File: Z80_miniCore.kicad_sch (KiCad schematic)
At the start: 37 parts, among them J1 ICSP, J2 UART, J3 I2C, J7 USB_B_Mini, SW1 ON|OFF, SW2 Z80_RESET, U1 Z84C00/PLCC, U2 PIC1-MMU, U3 AS6C4008-55PCN, U4 SST39SF010, U5 74HC595, U6 74HC595, U7 74HC595, Y1 CANNED-DIP8, Y2 Crystal

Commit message: add footprints for 595 + SST39SF
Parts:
- U4: footprint (none) -> Package_DIP:DIP-32_W15.24mm
- U5, U6, U7: footprint (none) -> Package_DIP:DIP-16_W7.62mm
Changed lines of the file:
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@@
 			)
 		)
-		(property "Footprint" ""
+		(property "Footprint" "Package_DIP:DIP-16_W7.62mm"
 			(at 152.4 128.27 0)
 			(hide yes)
@@
 			)
 		)
-		(property "Footprint" ""
+		(property "Footprint" "Package_DIP:DIP-32_W15.24mm"
 			(at 172.72 49.53 0)
 			(hide yes)
@@
 			)
 		)
-		(property "Footprint" ""
+		(property "Footprint" "Package_DIP:DIP-16_W7.62mm"
 			(at 114.3 128.27 0)
 			(hide yes)
@@
 			)
 		)
-		(property "Footprint" ""
+		(property "Footprint" "Package_DIP:DIP-16_W7.62mm"
 			(at 77.47 128.27 0)
 			(hide yes)

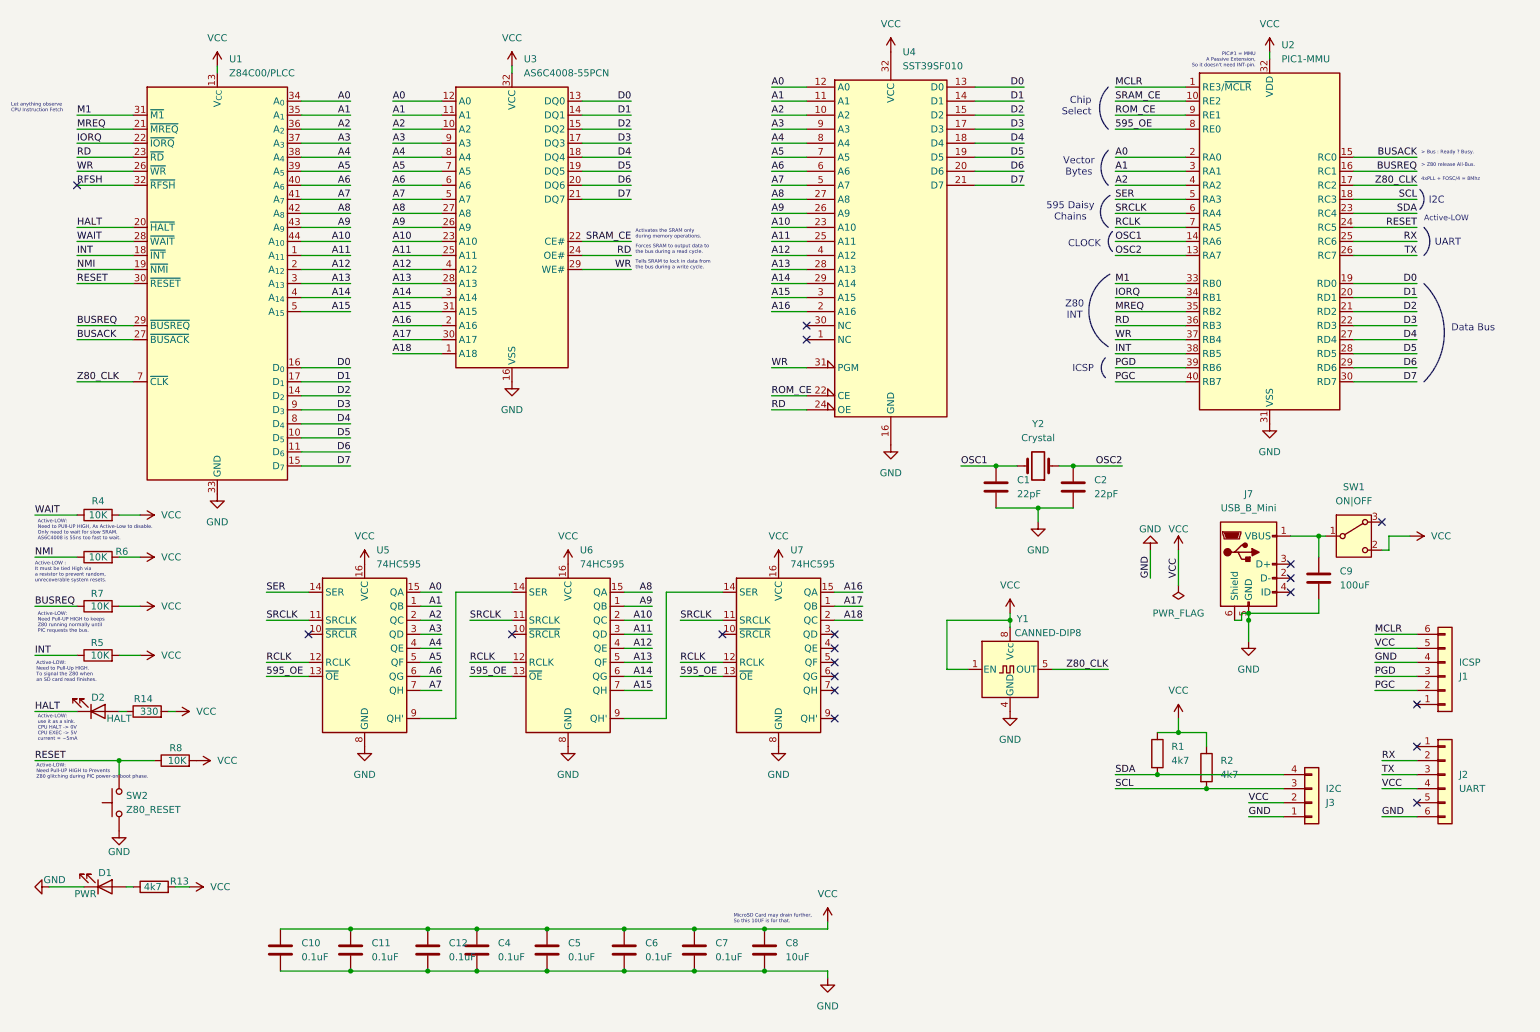
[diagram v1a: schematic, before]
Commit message: Remove Daisy Chain.
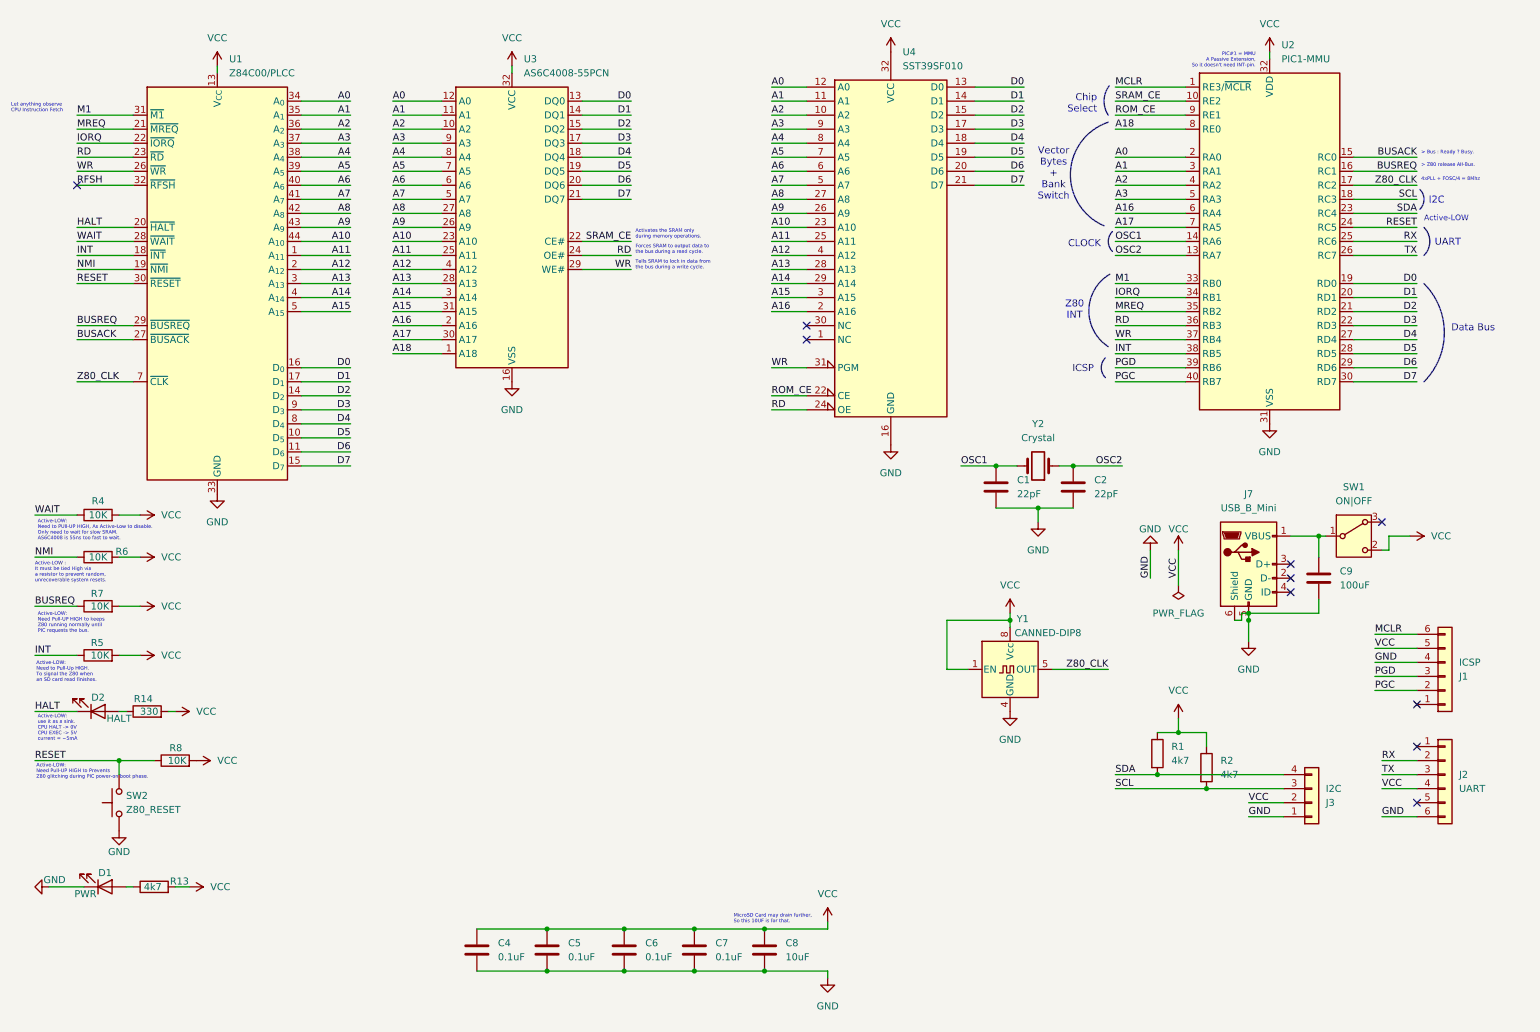
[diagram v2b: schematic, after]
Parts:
- removed C10, C11, C12: 0.1uF, Capacitor_THT:C_Disc_D3.4mm_W2.1mm_P2.50mm, symbol Device:C
- removed U5, U6, U7: 74HC595, Package_DIP:DIP-16_W7.62mm, symbol 74xx:74HC595
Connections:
- net 595_OE is gone; now on net A18: U2.8 (RE0)
- net RCLK is gone; now on net A17: U2.7 (RA5)
- net SER is gone; now on net A3: U2.5 (RA3)
- net SRCLK is gone; now on net A16: U2.6 (RA4)
- no-connect marks 19 -> 10
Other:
- note added: "Vector Bytes + Bank Switch"
- note removed: "595 Daisy Chains"
- note removed: "Vector Bytes"

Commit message: Add PIC2 as LOADER.
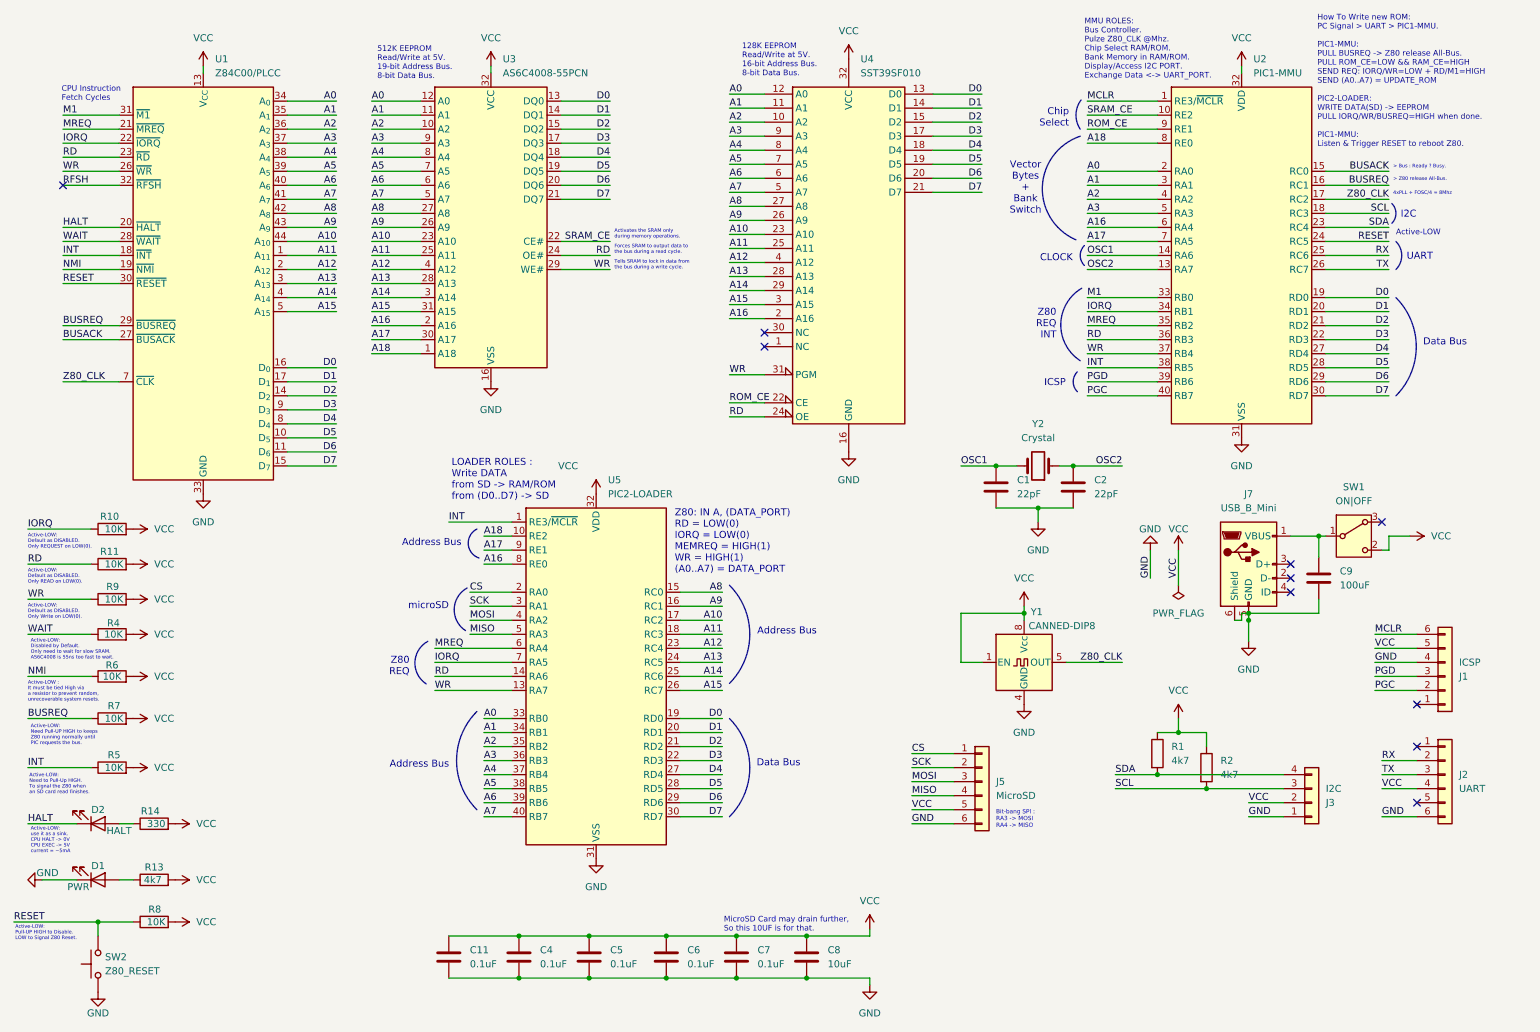
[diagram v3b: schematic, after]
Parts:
- added C11: 0.1uF, Capacitor_THT:C_Disc_D3.4mm_W2.1mm_P2.50mm, symbol Device:C
- added J5: MicroSD, Connector_PinSocket_2.54mm:PinSocket_1x06_P2.54mm_Vertical, symbol Connector_Generic:Conn_01x06
- added R10, R11, R9: 10K, Resistor_THT:R_Axial_DIN0207_L6.3mm_D2.5mm_P10.16mm_Horizontal, symbol Device:R
- added U5: PIC2-LOADER, Package_DIP:DIP-40_W15.24mm, symbol MCU_Microchip_PIC18:PIC18F4520-xP
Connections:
- net A0: now also U5.33 (RB0)
- net A1: now also U5.34 (RB1)
- net A10: now also U5.17 (RC2)
- net A11: now also U5.18 (RC3)
- net A12: now also U5.23 (RC4)
- net A13: now also U5.24 (RC5)
- net A14: now also U5.25 (RC6)
- net A15: now also U5.26 (RC7)
- net A16: now also U5.8 (RE0)
- net A17: now also U5.9 (RE1)
- net A18: now also U5.10 (RE2)
- net A2: now also U5.35 (RB2)
- net A3: now also U5.36 (RB3)
- net A4: now also U5.37 (RB4)
- net A5: now also U5.38 (RB5)
- net A6: now also U5.39 (RB6)
- net A7: now also U5.40 (RB7)
- net A8: now also U5.15 (RC0)
- net A9: now also U5.16 (RC1)
- net D0: now also U5.19 (RD0)
- net D1: now also U5.20 (RD1)
- net D2: now also U5.21 (RD2)
- net D3: now also U5.22 (RD3)
- net D4: now also U5.27 (RD4)
- net D5: now also U5.28 (RD5)
- net D6: now also U5.29 (RD6)
- net D7: now also U5.30 (RD7)
- net GND: now also C11.1, J5.6 (Pin_6), U5.12 (VSS), U5.31 (VSS)
- net INT: now also U5.1 (RE3/~{MCLR})
- net IORQ: now also R10.1, U5.7 (RA5)
- net MREQ: now also U5.6 (RA4)
- net RD: now also R11.1, U5.14 (RA6)
- net VCC: now also C11.2, J5.5 (Pin_5), R10.2, R11.2, R9.2, U5.11 (VDD), U5.32 (VDD)
- net WR: now also R9.1, U5.13 (RA7)
- new net CS: J5.1 (Pin_1), U5.2 (RA0)
- new net MISO: J5.4 (Pin_4), U5.5 (RA3)
- new net MOSI: J5.3 (Pin_3), U5.4 (RA2)
- new net SCK: J5.2 (Pin_2), U5.3 (RA1)
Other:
- note added: "128K EEPROM Read/Write at 5V. 16-bit Address Bus. 8-bit Data Bus."
- note added: "512K EEPROM Read/Write at 5V. 19-bit Address Bus. 8-bit Data Bus."
- note added: "Active-LOW: Default as DISABLED. Only READ on LOW(0)."
- note added: "Active-LOW: Default as DISABLED. Only REQUEST on LOW(0)."
- note added: "Active-LOW: Default as DISABLED. Only Write on LOW(0)."
- note added: "Active-LOW: Disabled by Default. Only need to wait for slow SRAM. AS6C4008 is 55ns too fast to wait."
- note added: "Active-LOW: Pull-UP HIGH to Disable. LOW to Signal Z80 Reset."
- note added: "Address Bus"
- note added: "Bit-bang SPI : RA3 -> MOSI RA4 -> MISO"
- note added: "CPU Instruction Fetch Cycles"
- note added: "How To Write new ROM: PC Signal > UART > PIC1-MMU. PIC1-MMU: PULL BUSREQ -> Z80 release All-Bus. PULL ROM_CE=LOW && RAM_CE=HIGH SEND REQ: IORQ/WR=LOW + RD/M1=HIGH SEND (A0..A7) = UPDATE_ROM PIC2-LOADER: WRITE DATA(SD) -> EEPROM PULL IORQ/WR/BUSREQ=HIGH when done. PIC1-MMU: Listen & Trigger RESET to reboot Z80."
- note added: "LOADER ROLES : Write DATA from SD -> RAM/ROM from (D0..D7) -> SD"
- note added: "MMU ROLES: Bus Controller. Pulze Z80_CLK @Mhz. Chip Select RAM/ROM. Bank Memory in RAM/ROM. Display/Access I2C PORT. Exchange Data <-> UART_PORT."
- note added: "Z80 REQ"
- note added: "Z80 REQ INT"
- note added: "Z80: IN A, (DATA_PORT) RD = LOW(0) IORQ = LOW(0) MEMREQ = HIGH(1) WR = HIGH(1) (A0..A7) = DATA_PORT"
- note added: "microSD"
- note removed: "Active-LOW: Need Pull-UP HIGH to Prevents Z80 glitching during PIC power-on boot phase."
- note removed: "Active-LOW: Need to PUll-UP HIGH, As Active-Low to disable. Only need to wait for slow SRAM. AS6C4008 is 55ns too fast to wait."
- note removed: "Let anything observe CPU Instruction Fetch"
- note removed: "PIC#1 = MMU A Passive Extension, So it doesn't need INT-pin."
- note removed: "Z80 INT"
- moved on the sheet: C4, C5, C6, C7, C8, D1, D2, R13, R14, R4, R5, R6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

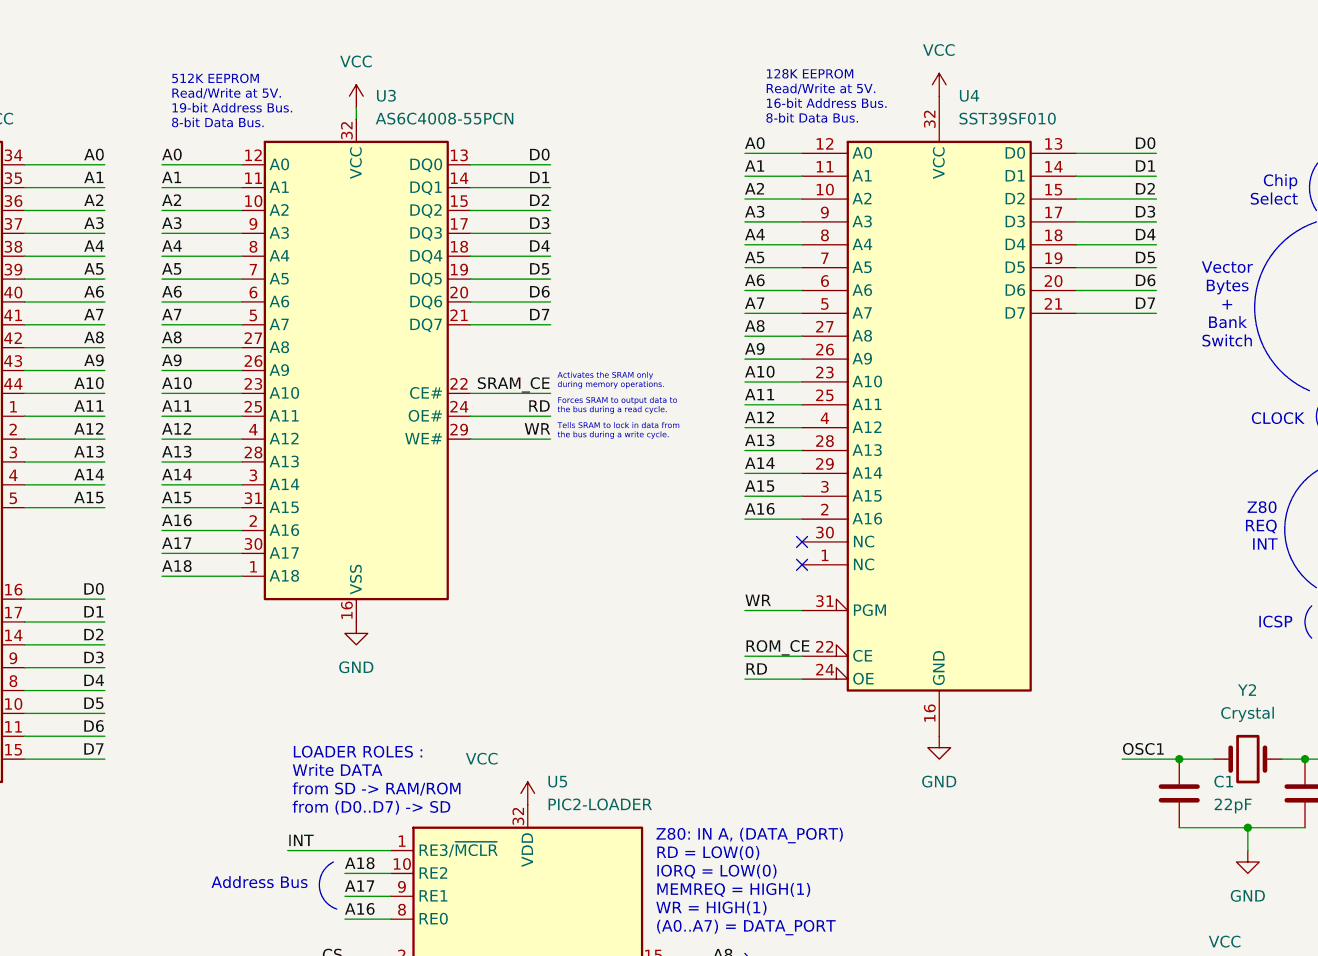
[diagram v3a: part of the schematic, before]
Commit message: added 2nd PIC as LOADER.
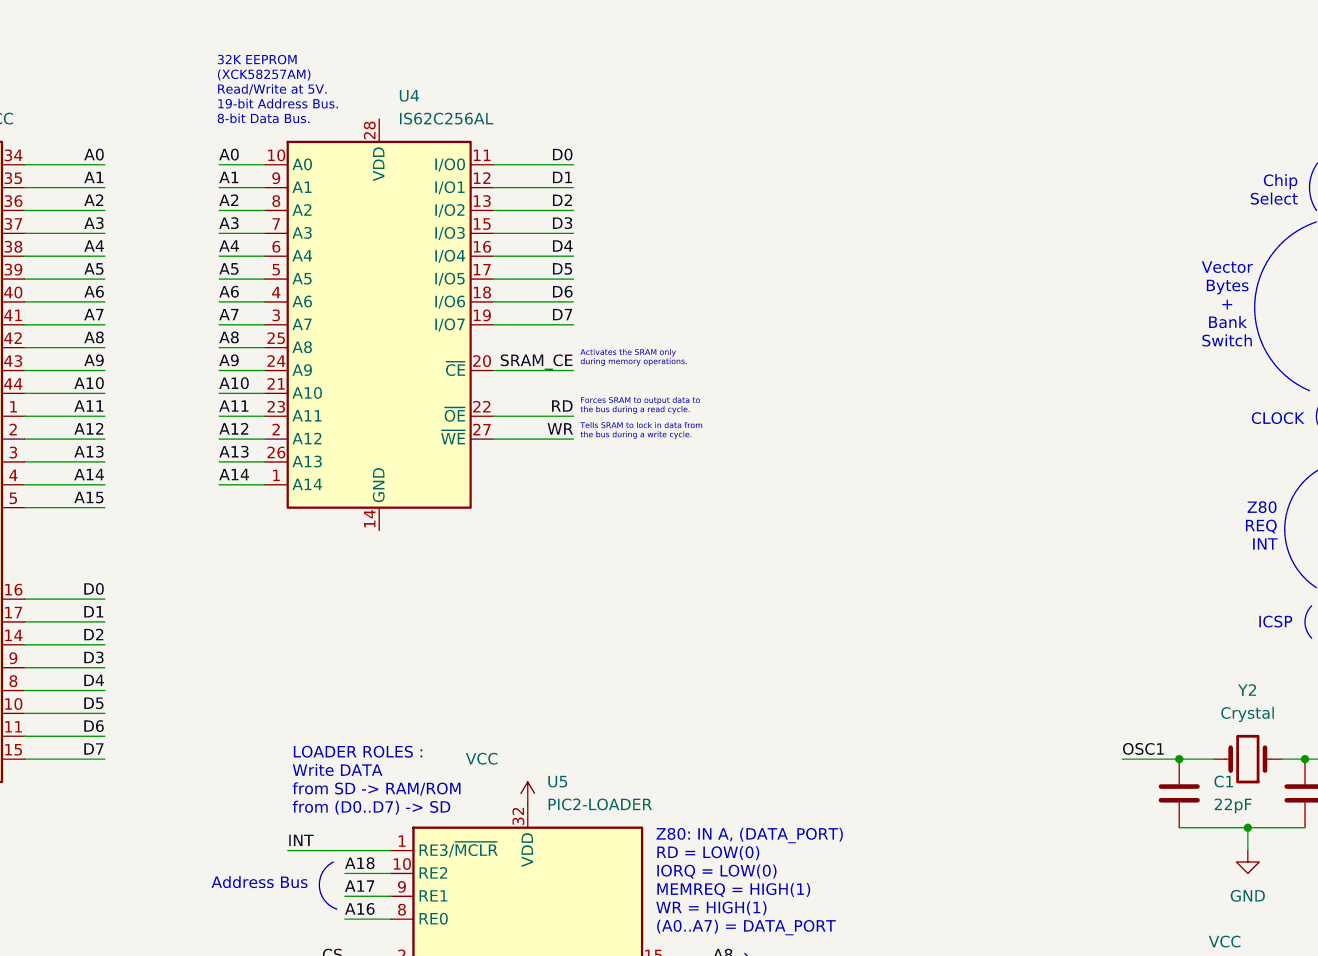
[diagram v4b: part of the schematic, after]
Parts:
- removed U3: AS6C4008-55PCN, Package_DIP:DIP-32_W15.24mm, symbol Memory_RAM:AS6C4008-55PCN
- removed U4: SST39SF010, Package_DIP:DIP-32_W15.24mm, symbol Memory_Flash:SST39SF010
- added U4: IS62C256AL, Package_SO:SOP-28_8.4x18.16mm_P1.27mm, symbol Memory_RAM:IS62C256AL
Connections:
- net A0: now also U4.10 (A0)
- net A1: now also U4.9 (A1)
- net A10: now also U4.21 (A10)
- net A11: now also U4.23 (A11)
- net A12: now also U4.2 (A12)
- net A13: now also U4.26 (A13)
- net A14: now also U4.1 (A14)
- net A2: now also U4.8 (A2)
- net A3: now also U4.7 (A3)
- net A4: now also U4.6 (A4)
- net A5: now also U4.5 (A5)
- net A6: now also U4.4 (A6)
- net A7: now also U4.3 (A7)
- net A8: now also U4.25 (A8)
- net A9: now also U4.24 (A9)
- net D0: now also U4.11 (I/O0)
- net D1: now also U4.12 (I/O1)
- net D2: now also U4.13 (I/O2)
- net D3: now also U4.15 (I/O3)
- net D4: now also U4.16 (I/O4)
- net D5: now also U4.17 (I/O5)
- net D6: now also U4.18 (I/O6)
- net D7: now also U4.19 (I/O7)
- net RD: now also U4.22 (~{OE})
- net SRAM_CE: now also U4.20 (~{CE})
- net WR: now also U4.27 (~{WE})
- no-connect marks 10 -> 8
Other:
- note added: "32K EEPROM (XCK58257AM) Read/Write at 5V. 19-bit Address Bus. 8-bit Data Bus."
- note removed: "128K EEPROM Read/Write at 5V. 16-bit Address Bus. 8-bit Data Bus."
- note removed: "512K EEPROM Read/Write at 5V. 19-bit Address Bus. 8-bit Data Bus."
